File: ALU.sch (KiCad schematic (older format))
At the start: 30 parts, among them U44 74LS245, U45 74LS00, U46 74LS86, U47 74LS86, U48 74LS86, U49 74LS00, U50 74LS86, U51 74HC02, U52 74LS00, U53 74LS00, U54 74LS283, U55 74LS85, U56 74LS283, U57 74LS245, U58 74LS85, U59 74LS245, U60 74LS283, U61 74LS85, U62 74LS173, U63 74LS283, U64 74LS245, U65 74LS85

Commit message: fixed more errors
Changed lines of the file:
@@
-$EndComp
-$Comp
-L 16bitCpu-rescue:+5V-power #PWR?
-U 1 1 60667C5F
-P 14100 17800
-AR Path="/60667C5F" Ref="#PWR?"  Part="1"
-AR Path="/5F5F4A69/60667C5F" Ref="#PWR0177"  Part="1"
-F 0 "#PWR0177" H 14100 17650 50  0001 C CNN
-F 1 "+5V" H 14115 17973 50  0000 C CNN
-F 2 "" H 14100 17800 50  0001 C CNN
-F 3 "" H 14100 17800 50  0001 C CNN
-	1    14100 17800
-	0    -1   -1   0
 $EndComp
 $Comp
@@
 Wire Wire Line
 	5350 18650 4900 18650
-$Comp
-L 16bitCpu-rescue:+5V-power #PWR0188
-U 1 1 5F826AFE
-P 18350 17850
-F 0 "#PWR0188" H 18350 17700 50  0001 C CNN
-F 1 "+5V" H 18365 18023 50  0000 C CNN
-F 2 "" H 18350 17850 50  0001 C CNN
-F 3 "" H 18350 17850 50  0001 C CNN
-	1    18350 17850
-	0    1    -1   0
-$EndComp
-Wire Wire Line
-	18200 17850 18350 17850
 Text HLabel 17700 18700 3    50   Output ~ 0
 ZF
@@
 	7050 10650 8600 10650
 Connection ~ 10450 4900
+$Comp
+L 16bitCpu-rescue:+5V-power #PWR?
+U 1 1 63E4B52F
+P 18200 17850
+AR Path="/63E4B52F" Ref="#PWR?"  Part="1"
+AR Path="/5F5F4A69/63E4B52F" Ref="#PWR0136"  Part="1"
+F 0 "#PWR0136" H 18200 17700 50  0001 C CNN
+F 1 "+5V" H 18215 18023 50  0000 C CNN
+F 2 "" H 18200 17850 50  0001 C CNN
+F 3 "" H 18200 17850 50  0001 C CNN
+	1    18200 17850
+	0    1    1    0
+$EndComp
+$Comp
+L 16bitCpu-rescue:+5V-power #PWR?
+U 1 1 63F666EC
+P 14100 17800
+AR Path="/63F666EC" Ref="#PWR?"  Part="1"
+AR Path="/5F5F4A69/63F666EC" Ref="#PWR0177"  Part="1"
+F 0 "#PWR0177" H 14100 17650 50  0001 C CNN
+F 1 "+5V" H 14115 17973 50  0000 C CNN
+F 2 "" H 14100 17800 50  0001 C CNN
+F 3 "" H 14100 17800 50  0001 C CNN
+	1    14100 17800
+	0    -1   -1   0
+$EndComp
 $EndSCHEMATC

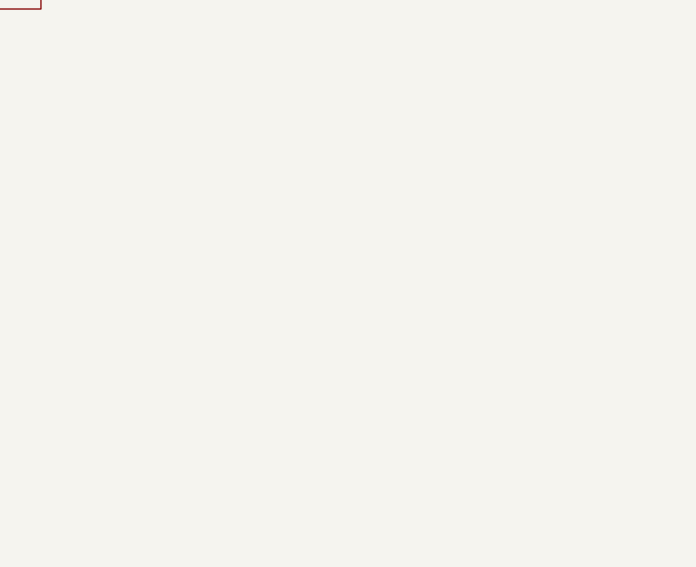
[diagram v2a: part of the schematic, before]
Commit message: added power caps
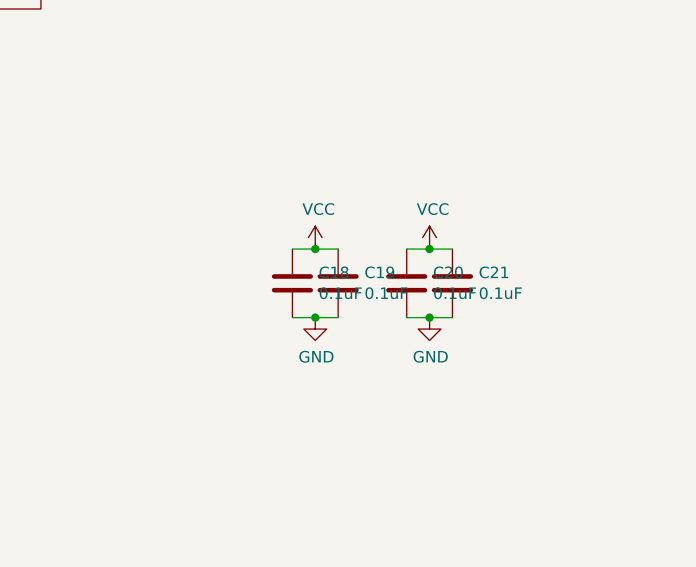
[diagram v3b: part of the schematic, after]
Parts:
- added C18, C19, C20, C21: 0.1uF, Capacitor_THT:CP_Axial_L10.0mm_D4.5mm_P15.00mm_Horizontal, symbol Device:C
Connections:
- net GND: now also C18.2, C19.2, C20.2, C21.2
- new net VCC: C18.1, C19.1, C20.1, C21.1
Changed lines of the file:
@@
 	0    -1   -1   0
 $EndComp
+$Comp
+L 16bitCpu-rescue:VCC-power #PWR?
+U 1 1 5FB50338
+P 19700 2800
+AR Path="/5FB50338" Ref="#PWR?"  Part="1"
+AR Path="/5F5F4A69/5FB50338" Ref="#PWR0271"  Part="1"
+F 0 "#PWR0271" H 19700 2650 50  0001 C CNN
+F 1 "VCC" H 19715 2973 50  0000 C CNN
+F 2 "" H 19700 2800 50  0001 C CNN
+F 3 "" H 19700 2800 50  0001 C CNN
+	1    19700 2800
+	1    0    0    -1
+$EndComp
+$Comp
+L 16bitCpu-rescue:GND-power #PWR?
+U 1 1 5FB5033E
+P 19700 3100
+AR Path="/5FB5033E" Ref="#PWR?"  Part="1"
+AR Path="/5F75E433/5FB5033E" Ref="#PWR?"  Part="1"
+AR Path="/5F5F4A69/5FB5033E" Ref="#PWR0272"  Part="1"
+F 0 "#PWR0272" H 19700 2850 50  0001 C CNN
+F 1 "GND" H 19705 2927 50  0000 C CNN
+F 2 "" H 19700 3100 50  0001 C CNN
+F 3 "" H 19700 3100 50  0001 C CNN
+	1    19700 3100
+	1    0    0    -1
+$EndComp
+Wire Wire Line
+	19700 2800 19800 2800
+Wire Wire Line
+	19800 3100 19700 3100
+$Comp
+L Device:C C?
+U 1 1 5FB50346
+P 19600 2950
+AR Path="/5F75E433/5FB50346" Ref="C?"  Part="1"
+AR Path="/5F5F4A69/5FB50346" Ref="C18"  Part="1"
+F 0 "C18" H 19715 2996 50  0000 L CNN
+F 1 "0.1uF" H 19715 2905 50  0000 L CNN
+F 2 "Capacitor_THT:CP_Axial_L10.0mm_D4.5mm_P15.00mm_Horizontal" H 19638 2800 50  0001 C CNN
+F 3 "" H 19600 2950 50  0001 C CNN
+	1    19600 2950
+	1    0    0    -1
+$EndComp
+Wire Wire Line
+	19700 2800 19600 2800
+Connection ~ 19700 2800
+Wire Wire Line
+	19600 3100 19700 3100
+Connection ~ 19700 3100
+$Comp
+L Device:C C?
+U 1 1 5FB50350
+P 19800 2950
+AR Path="/5F75E433/5FB50350" Ref="C?"  Part="1"
+AR Path="/5F5F4A69/5FB50350" Ref="C19"  Part="1"
+F 0 "C19" H 19915 2996 50  0000 L CNN
+F 1 "0.1uF" H 19915 2905 50  0000 L CNN
+F 2 "Capacitor_THT:CP_Axial_L10.0mm_D4.5mm_P15.00mm_Horizontal" H 19838 2800 50  0001 C CNN
+F 3 "" H 19800 2950 50  0001 C CNN
+	1    19800 2950
+	1    0    0    -1
+$EndComp
+$Comp
+L 16bitCpu-rescue:VCC-power #PWR?
+U 1 1 5FBDD7DF
+P 20200 2800
+AR Path="/5FBDD7DF" Ref="#PWR?"  Part="1"
+AR Path="/5F5F4A69/5FBDD7DF" Ref="#PWR0273"  Part="1"
+F 0 "#PWR0273" H 20200 2650 50  0001 C CNN
+F 1 "VCC" H 20215 2973 50  0000 C CNN
+F 2 "" H 20200 2800 50  0001 C CNN
+F 3 "" H 20200 2800 50  0001 C CNN
+	1    20200 2800
+	1    0    0    -1
+$EndComp
+$Comp
+L 16bitCpu-rescue:GND-power #PWR?
+U 1 1 5FBDD7E5
+P 20200 3100
+AR Path="/5FBDD7E5" Ref="#PWR?"  Part="1"
+AR Path="/5F75E433/5FBDD7E5" Ref="#PWR?"  Part="1"
+AR Path="/5F5F4A69/5FBDD7E5" Ref="#PWR0274"  Part="1"
+F 0 "#PWR0274" H 20200 2850 50  0001 C CNN
+F 1 "GND" H 20205 2927 50  0000 C CNN
+F 2 "" H 20200 3100 50  0001 C CNN
+F 3 "" H 20200 3100 50  0001 C CNN
+	1    20200 3100
+	1    0    0    -1
+$EndComp
+Wire Wire Line
+	20200 2800 20300 2800
+Wire Wire Line
+	20300 3100 20200 3100
+$Comp
+L Device:C C?
+U 1 1 5FBDD7ED
+P 20100 2950
+AR Path="/5F75E433/5FBDD7ED" Ref="C?"  Part="1"
+AR Path="/5F5F4A69/5FBDD7ED" Ref="C20"  Part="1"
+F 0 "C20" H 20215 2996 50  0000 L CNN
+F 1 "0.1uF" H 20215 2905 50  0000 L CNN
+F 2 "Capacitor_THT:CP_Axial_L10.0mm_D4.5mm_P15.00mm_Horizontal" H 20138 2800 50  0001 C CNN
+F 3 "" H 20100 2950 50  0001 C CNN
+	1    20100 2950
+	1    0    0    -1
+$EndComp
+Wire Wire Line
+	20200 2800 20100 2800
+Connection ~ 20200 2800
+Wire Wire Line
+	20100 3100 20200 3100
+Connection ~ 20200 3100
+$Comp
+L Device:C C?
+U 1 1 5FBDD7F7
+P 20300 2950
+AR Path="/5F75E433/5FBDD7F7" Ref="C?"  Part="1"
+AR Path="/5F5F4A69/5FBDD7F7" Ref="C21"  Part="1"
+F 0 "C21" H 20415 2996 50  0000 L CNN
+F 1 "0.1uF" H 20415 2905 50  0000 L CNN
+F 2 "Capacitor_THT:CP_Axial_L10.0mm_D4.5mm_P15.00mm_Horizontal" H 20338 2800 50  0001 C CNN
+F 3 "" H 20300 2950 50  0001 C CNN
+	1    20300 2950
+	1    0    0    -1
+$EndComp
 $EndSCHEMATC

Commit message: added display
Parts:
- renumbered D103 to D81, D104 to D82, D105 to D83, D106 to D84, R110 to R87, R111 to R88, R112 to R89, R113 to R90, U44 to U37, U45 to U38, U46 to U39, U47 to U40, U48 to U41, U49 to U42, U50 to U43, U51 to U44, U52 to U45, U53 to U46, U54 to U47, U55 to U48, U56 to U49, U57 to U50, U58 to U51, U59 to U52, U60 to U53, U61 to U54, U62 to U55, U63 to U56, U64 to U57, U65 to U58
